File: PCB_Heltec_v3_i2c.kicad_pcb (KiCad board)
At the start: 2 copper layers, 33 x 72.4 mm, 13 parts, among them J1 i2c, J2 i2c, J3 i2c, J4 SPI, J5 Conn_01x04_Pin, J6 PINHD_1x4_Female, J7 PINHD_1x4_Female, U1 ESP32_LORA_V2.0

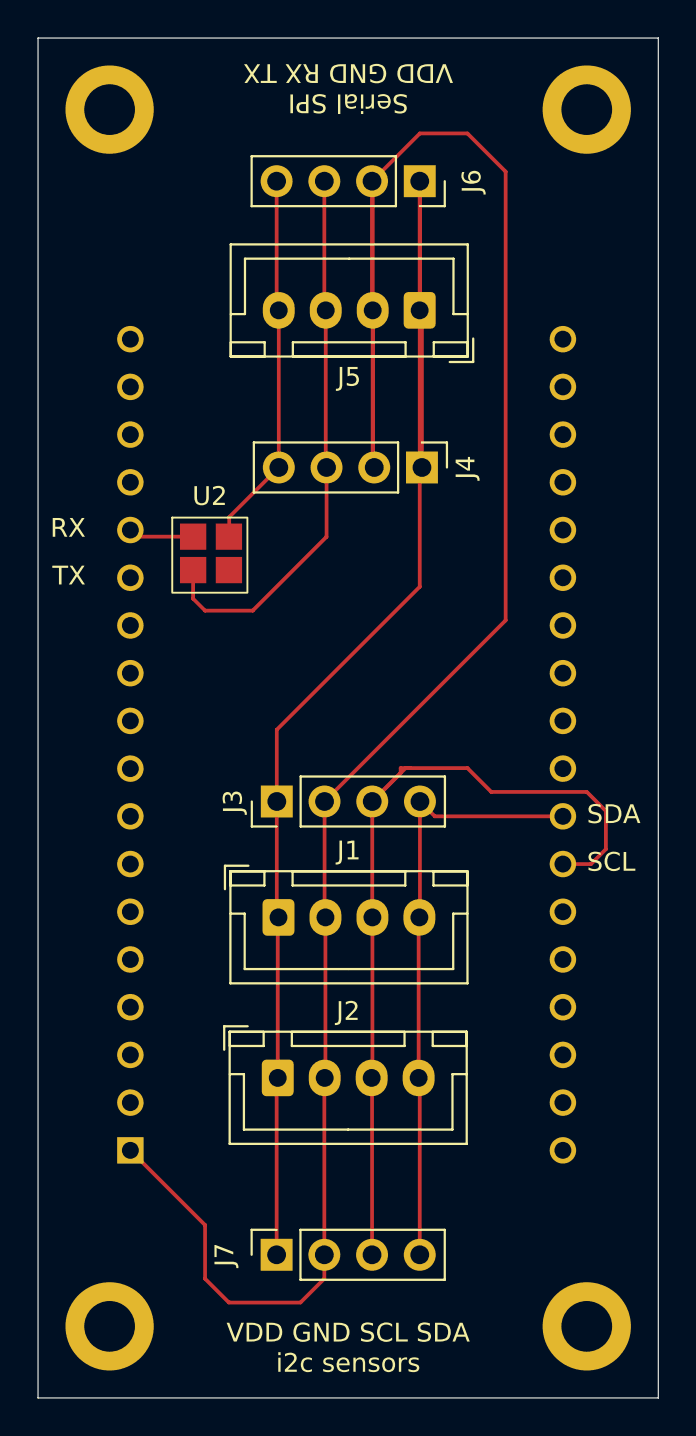
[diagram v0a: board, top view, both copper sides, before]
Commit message: fix CDD net routing, replace rx/tx mux with pin header instead smd pads, reduce board width
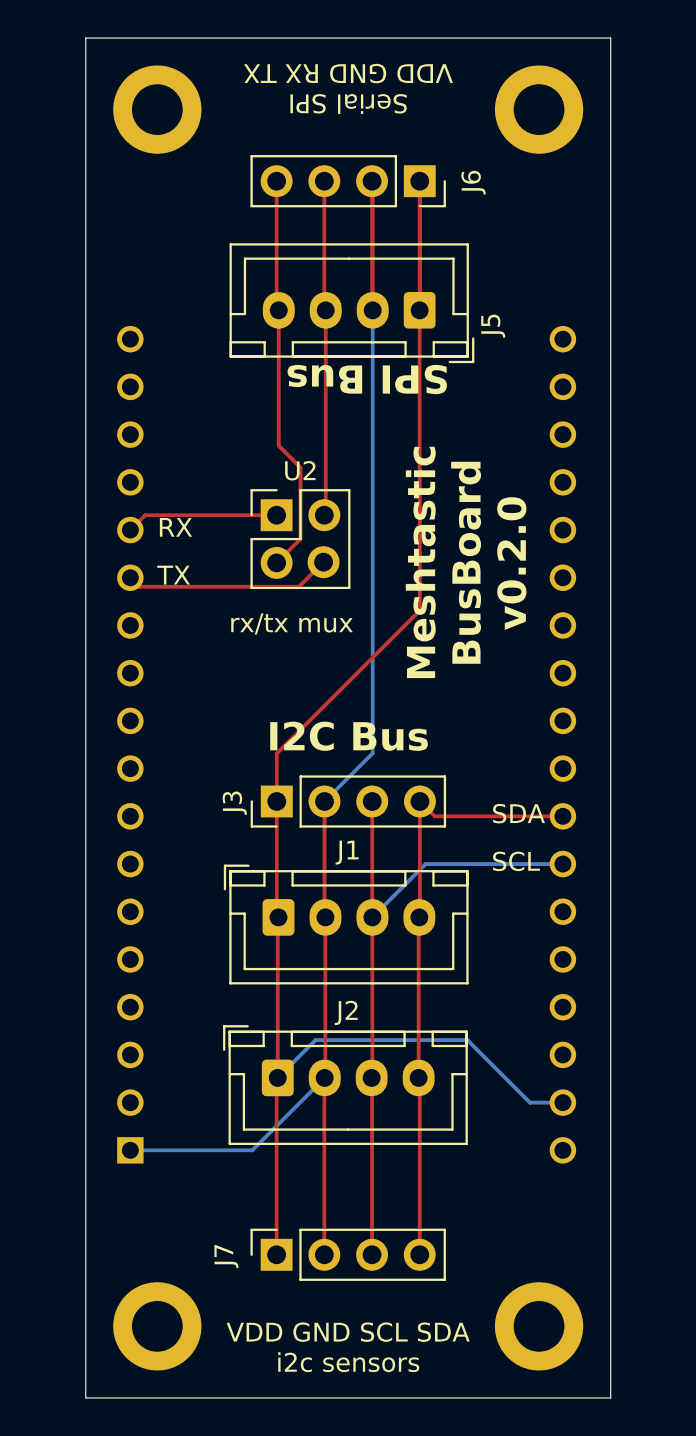
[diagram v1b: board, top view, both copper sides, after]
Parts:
- removed J4: SPI, Connector_PinHeader_2.54mm:PinHeader_1x04_P2.54mm_Vertical
- U2: footprint PCB_Heltec_v3_i2c:poka-yoke_rxtx -> Connector_PinHeader_2.54mm:PinHeader_2x02_P2.54mm_Vertical
- moved U2 3.59 mm to (68.6, 95.2)
- moved ? 2.54 mm to (82.5, 138.4)
- moved ? 2.54 mm to (82.5, 73.7)
- moved ? 2.54 mm to (62.2, 138.4)
- moved REF** 2.54 mm to (62.2, 73.7)
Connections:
- U1 pad J3_2: Net-(U1-3V3-PadJ3_2) -> VDD
- U1 pad J3_3: Net-(U1-3V3-PadJ3_2) -> VDD
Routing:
- net GND: track 118.4 -> 77.9 mm
- net /SCL: track 45.8 -> 35.5 mm
- net VDD: track 76.1 -> 86.0 mm
- net RX: track 23.9 -> 30.2 mm
- net TX: track 30.3 -> 29.7 mm
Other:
- board size 33 x 72.4 mm -> 27.9 x 72.4 mm
- board text added: "GND"
- board text added: "I2C Bus"
- board text added: "Meshtastic BusBoard v0.2.0"
- board text added: "SPI Bus"
- board text added: "VDD"
- board text added: "rx/tx mux"
